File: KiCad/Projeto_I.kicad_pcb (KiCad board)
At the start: 2 copper layers, 16.5 x 21.5 mm, 3 parts

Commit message: AUla do dia 04/04/2025
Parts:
- added C1: 22p, Capacitor_THT:C_Rect_L7.0mm_W2.5mm_P5.00mm, F.Cu at (196.5, 100.5)
- added C10: 100n, Capacitor_THT:C_Rect_L7.0mm_W2.5mm_P5.00mm, F.Cu at (112.6, 87.9)
- added C11: 10u, Capacitor_THT:CP_Radial_D10.0mm_P3.80mm, F.Cu at (123.6, 78.9)
- added C2: 22p, Capacitor_THT:C_Rect_L7.0mm_W2.5mm_P5.00mm, F.Cu at (192.0, 81.0)
- added C3: 220n, Capacitor_THT:C_Rect_L7.0mm_W2.5mm_P5.00mm, F.Cu at (112.6, 63.6)
- added C4: 100n, Capacitor_THT:C_Rect_L7.0mm_W2.5mm_P5.00mm, F.Cu at (112.6, 67.7)
- added C5: 10n, Capacitor_THT:C_Rect_L7.0mm_W2.5mm_P5.00mm, F.Cu at (112.6, 71.7)
- added C6: 100n, Capacitor_THT:C_Rect_L7.0mm_W2.5mm_P5.00mm, F.Cu at (112.6, 75.8)
- added C7: 10n, Capacitor_THT:C_Rect_L7.0mm_W2.5mm_P5.00mm, F.Cu at (112.6, 79.8)
- added C8: 10u, Capacitor_THT:CP_Radial_D10.0mm_P3.80mm, F.Cu at (123.6, 67.4)
- added C9: 100n, Capacitor_THT:C_Rect_L7.0mm_W2.5mm_P5.00mm, F.Cu at (112.6, 83.9)
- added D1: RD0, LED_THT:LED_D3.0mm, F.Cu at (132.9, 64.3)
- added D2: RD0, LED_THT:LED_D3.0mm, F.Cu at (132.9, 69.8)
- added D3: RD0, LED_THT:LED_D3.0mm, F.Cu at (132.9, 75.3)
- added D4: RD0, LED_THT:LED_D3.0mm, F.Cu at (132.9, 80.8)
- added D5: RD0, LED_THT:LED_D3.0mm, F.Cu at (138.8, 64.3)
- added D6: RD0, LED_THT:LED_D3.0mm, F.Cu at (138.8, 69.8)
- added D7: D_Small, Diode_THT:D_DO-41_SOD81_P10.16mm_Horizontal, F.Cu at (129.8, 98.7)
- added D8: RD0, LED_THT:LED_D3.0mm, F.Cu at (138.8, 75.3)
- added F1: MF-MSMF050-2, Library:FUSM4632X85, F.Cu at (95.5, 116.6)
- added J1: PORTA, Connector_PinSocket_2.54mm:PinSocket_1x06_P2.54mm_Vertical, F.Cu at (102.4, 104.4)
- added J2: PORTB, Connector_PinSocket_2.54mm:PinSocket_1x08_P2.54mm_Vertical, F.Cu at (113.2, 104.9)
- added J3: PORTC, Connector_PinSocket_2.54mm:PinSocket_1x07_P2.54mm_Vertical, F.Cu at (117.8, 104.9)
- added J4: USB_B_Micro, Connector_USB:USB_Micro-AB_Molex_47590-0001, F.Cu at (233.2, 115.8)
- added J5: Barrel_Jack_Switch, Connector_BarrelJack:BarrelJack_Horizontal, F.Cu at (125.4, 95.3)
- added Q1: PMOS, Package_TO_SOT_THT:TO-92L_HandSolder, F.Cu at (93.4, 122.7)
- added R10: 10k, Resistor_THT:R_Axial_DIN0207_L6.3mm_D2.5mm_P7.62mm_Horizontal, F.Cu at (101.7, 100.1)
- added R4: 10K, Resistor_THT:R_Axial_DIN0207_L6.3mm_D2.5mm_P7.62mm_Horizontal, F.Cu at (101.7, 75.8)
- added R5: 10K, Resistor_THT:R_Axial_DIN0207_L6.3mm_D2.5mm_P7.62mm_Horizontal, F.Cu at (101.7, 79.8)
- added R6: 10K, Resistor_THT:R_Axial_DIN0207_L6.3mm_D2.5mm_P7.62mm_Horizontal, F.Cu at (101.7, 83.9)
- added R7: 10K, Resistor_THT:R_Axial_DIN0207_L6.3mm_D2.5mm_P7.62mm_Horizontal, F.Cu at (101.7, 87.9)
- added R8: 470, Resistor_THT:R_Axial_DIN0207_L6.3mm_D2.5mm_P7.62mm_Horizontal, F.Cu at (101.7, 92.0)
- added R9: 10k, Resistor_THT:R_Axial_DIN0207_L6.3mm_D2.5mm_P7.62mm_Horizontal, F.Cu at (101.7, 96.0)
- added SW1: reset, Button_Switch_THT:SW_TH_Tactile_Omron_B3F-10xx, F.Cu at (83.3, 115.6)
- added U1: PIC18F4550-IP, Package_DIP:DIP-40_W15.24mm, F.Cu at (204.8, 59.4)
- added U2: LM7805, Package_TO_SOT_THT:TO-220-3_Vertical, F.Cu at (134.5, 87.4)
- added U3: LM358, Package_DIP:DIP-8_W7.62mm, F.Cu at (132.7, 104.7)
- added U4: AMS1117, Package_TO_SOT_SMD:SOT-223-3_TabPin2, F.Cu at (125.0, 119.9)
- added Y1: 16MHz, Crystal:Crystal_HC49-U_Vertical, F.Cu at (198.5, 93.5)
- R1: value 10k -> 10K
- R2: value 1k -> 10K
- R3: value 100 -> 10K
- moved R3 16.3 mm to (101.7, 71.7)
- moved R2 14.5 mm to (101.7, 67.7)
- moved R1 13.1 mm to (101.7, 63.6)
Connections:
- R1 pad 2: Earth -> Rst
- R2 pad 1: +5V -> RD0
- R2 pad 2: Earth -> Net-(D1-A)
- R3 pad 1: +5V -> RD1
- R3 pad 2: Earth -> Net-(D2-A)
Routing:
- net Earth: track 23.7 -> 69.8 mm
- net osc1: track 0.00 -> 15.9 mm
- net osc2: track 0.00 -> 15.4 mm
- net +5V: track 20.9 -> 19.2 mm
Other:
- board size 16.5 x 21.5 mm -> 103.5 x 64 mm

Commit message: Atualização da PCB
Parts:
- removed U2: LM7805, Package_TO_SOT_THT:TO-220-3_Vertical
- added D9: RD0, LED_THT:LED_D3.0mm, F.Cu at (89.4, 47.0)
- added U5: USBLC6-2SC6, Package_TO_SOT_SMD:SOT-23-6, F.Cu at (77.9, 84.3)
- added U6: AMS1117-5.0, Package_TO_SOT_SMD:SOT-223-3_TabPin2, F.Cu at (74.8, 108.9)
- C1, C2: footprint Capacitor_THT:C_Rect_L7.0mm_W2.5mm_P5.00mm -> Capacitor_THT:C_Disc_D5.0mm_W2.5mm_P2.50mm
- C11, C8: footprint Capacitor_THT:CP_Radial_D10.0mm_P3.80mm -> Capacitor_THT:CP_Radial_D5.0mm_P2.50mm
- J4: value USB_B_Micro -> USB
- Q1: footprint Package_TO_SOT_THT:TO-92L_HandSolder -> Package_TO_SOT_SMD:SOT-23
- moved J4 168.8 mm to (67.7, 83.1), turned to -90 degrees
- moved R5 154.1 mm to (254.0, 103.4), turned to -90 degrees
- moved R4 147.9 mm to (247.0, 103.5), turned to -90 degrees
- moved R7 139.1 mm to (240.0, 103.0), turned to -90 degrees
- moved R6 132.7 mm to (233.0, 103.2), turned to -90 degrees
- moved R3 128.2 mm to (225.9, 103.4), turned to -90 degrees
- moved D4 124.0 mm to (251.5, 117.0)
- moved R2 122.8 mm to (219.0, 103.9), turned to -90 degrees
- moved C10 119.5 mm to (227.5, 55.0)
- moved D3 119.1 mm to (244.5, 117.1)
- moved D6 109.4 mm to (237.5, 117.0)
- moved D5 105.7 mm to (230.5, 117.0)
- moved D2 102.1 mm to (223.5, 117.0)
- moved D1 98.8 mm to (216.5, 117.0)
- moved J3 96.3 mm to (209.6, 76.0), turned to -90 degrees
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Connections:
- F1 pad 2: +5V -> USB_VCC
- J4 pad 2: RC4 -> /USB_D-
- J4 pad 3: RC5 -> /USB_D+
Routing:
- net Earth: track 69.8 -> 0.00 mm
- net +5V: track 19.2 -> 0.00 mm
- net osc1: track 15.9 -> 0.00 mm
- net osc2: track 15.4 -> 0.00 mm
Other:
- board size 103.5 x 64 mm -> 149 x 63.5 mm

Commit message: Atualização PCB
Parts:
- removed D9: RD0, LED_THT:LED_D3.0mm
- moved C10 92.4 mm to (138.0, 78.0), turned to -90 degrees
- moved C3 84.8 mm to (131.0, 73.0), turned to -90 degrees
- moved C8 80.5 mm to (151.0, 103.5), turned to -90 degrees
- moved C11 76.5 mm to (150.0, 95.0)
- moved SW1 75.9 mm to (150.0, 116.5)
- moved D8 58.3 mm to (137.0, 69.0)
- moved D7 52.0 mm to (136.5, 103.2)
- moved J4 50.2 mm to (116.2, 70.2)
- moved U6 50.1 mm to (124.5, 102.0)
- moved U4 49.9 mm to (124.2, 89.5)
- moved U5 49.6 mm to (125.9, 71.8)
- moved J5 49.1 mm to (127.5, 113.5)
- moved R1 47.2 mm to (134.9, 120.0), turned to 0 degrees
- moved Q1 46.5 mm to (131.5, 82.4)
- moved F1 42.8 mm to (124.0, 79.0), turned to -90 degrees
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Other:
- board size 149 x 63.5 mm -> 128 x 63.5 mm

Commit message: Finalizção da PCB v1.1
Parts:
- U4: value AMS1117 -> AMS1117-3.3
- moved C2 2.12 mm to (188.0, 119.5)
- moved C1 1.95 mm to (201.0, 117.0)
- moved Y1 1.50 mm to (197.0, 110.5)
- moved J4 0.30 mm to (116.5, 70.2)
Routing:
- net +5V: track 0.00 -> 177.4 mm, vias 0 -> 1
- net Vusb: track 0.00 -> 108.0 mm, vias 0 -> 1
- net RC4: track 0.00 -> 104.8 mm
- net RC0: track 0.00 -> 103.0 mm
- net RC5: track 0.00 -> 99.8 mm
- net RC1: track 0.00 -> 98.0 mm
- net RC2: track 0.00 -> 91.7 mm
- net Earth: track 0.00 -> 41.3 mm
- net +3.3V: track 0.00 -> 40.7 mm
- net Rst: track 0.00 -> 35.4 mm
- net PwrIn: track 0.00 -> 32.7 mm
- net RD5: track 0.00 -> 28.4 mm
- net RC7: track 0.00 -> 25.8 mm
- net RC6: track 0.00 -> 25.8 mm
- net Net-(D7-K): track 0.00 -> 24.9 mm
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- added copper zone on B.Cu, net Earth
- added copper zone on F.Cu, net Earth
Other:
- board size 128 x 63.5 mm -> 123 x 63.5 mm

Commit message: .
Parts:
- added J6: Alimentação, Connector_PinSocket_2.54mm:PinSocket_1x04_P2.54mm_Vertical, F.Cu at (189.8, 122.0)
- D2: value RD0 -> RD1
- D3: value RD0 -> RD4
- D4: value RD0 -> RD5
- D5: value RD0 -> RD2
- D6: value RD0 -> RD3
- Q1: value PMOS -> FDN340P
- U4: value AMS1117-3.3 -> AMS1117
- moved C1 4.80 mm to (197.2, 114.0)
- moved C2 3.47 mm to (189.8, 116.5)
- moved C8 2.94 mm to (150.1, 106.3), turned to 0 degrees
- moved Y1 2.39 mm to (195.7, 108.5)
- moved R1 1.01 mm to (134.7, 121.0)
- moved C6 0.56 mm to (180.0, 113.2)
- moved C7 0.54 mm to (180.0, 108.3)
- moved D2 0.12 mm to (231.9, 113.7)
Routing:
- net +5V: track 177.4 -> 255.2 mm, vias 1 -> 0
- net +3.3V: track 40.7 -> 93.5 mm
- net Earth: track 41.3 -> 18.8 mm
- net Vusb: track 108.0 -> 103.2 mm, vias 1 -> 0
- net osc2: track 16.3 -> 12.0 mm
- net osc1: track 16.5 -> 12.8 mm
- net RD1: track 11.3 -> 13.6 mm
- net RC2: track 91.7 -> 92.9 mm
- net PwrIn: track 32.7 -> 33.7 mm
- net RD0: track 19.5 -> 20.2 mm
- net /USB_D-: track 5.31 -> 6.01 mm
- net /USB_D+: track 4.79 -> 5.49 mm
- net Net-(J4-VBUS): track 7.71 -> 8.41 mm
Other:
- board text added: "3.3V"
- board text added: "5V"
- board text added: "GND"
- board text added: "RA0"
- board text added: "RA1"
- board text added: "RA2"
- board text added: "RA3"
- board text added: "RA4"
- board text added: "RA5"
- board text added: "RB0"
- board text added: "RB1"
- board text added: "RB2"
- board text added: "RB3"
- board text added: "RB4"
- board text added: "RB5"
- board text added: "RB6"
- board text added: "RB7"
- board text added: "min: 7V max: 12V"

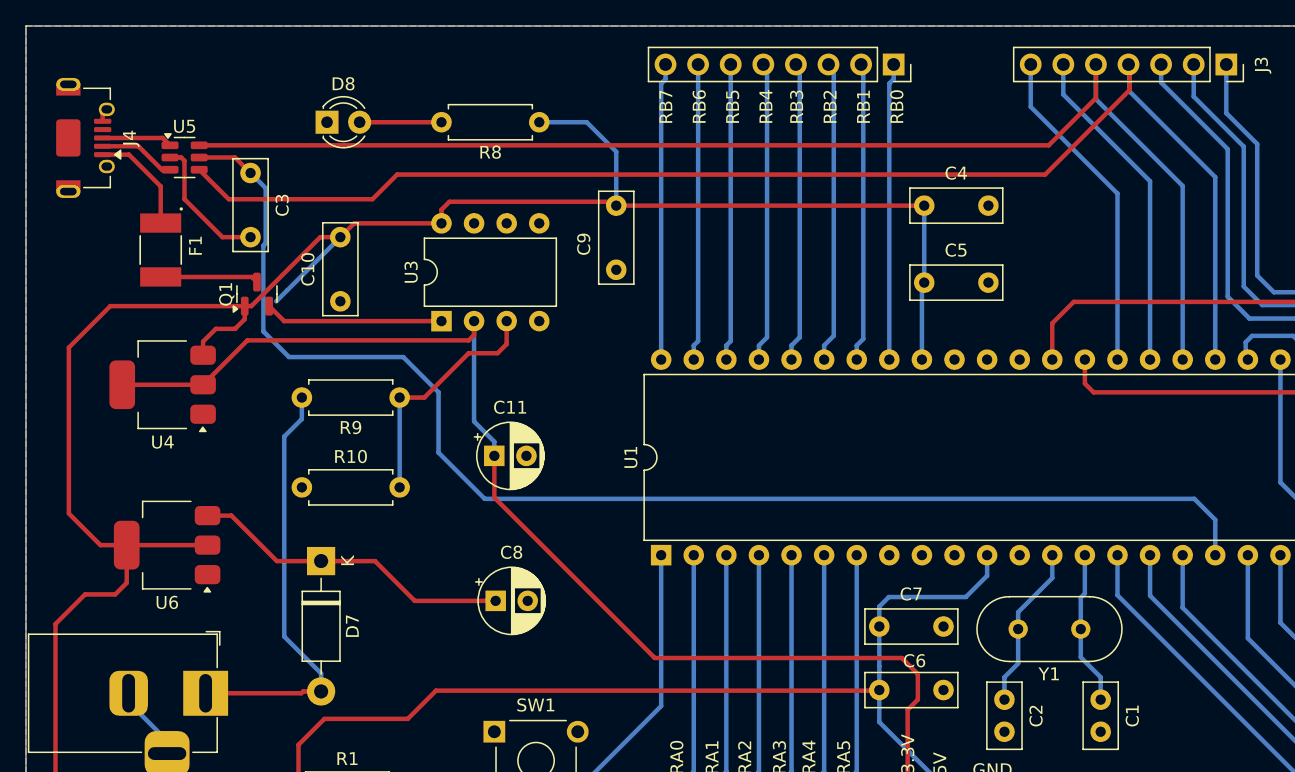
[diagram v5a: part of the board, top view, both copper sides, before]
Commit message: Atualização da PCB e conserto do esquemático do Transistor FDN340P
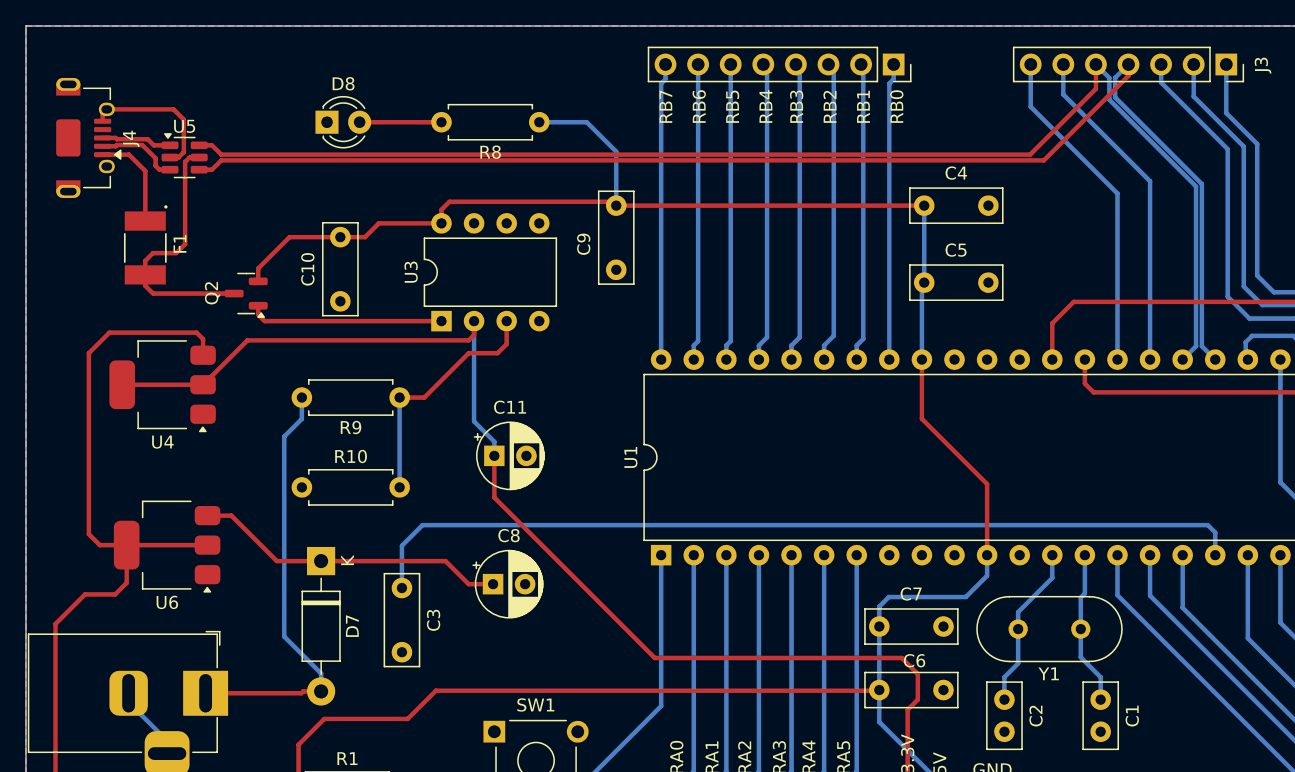
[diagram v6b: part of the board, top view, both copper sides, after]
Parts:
- removed Q1: FDN340P, Package_TO_SOT_SMD:SOT-23
- added Q2: FDN340P, Package_TO_SOT_SMD:SOT-23, F.Cu at (130.7, 82.3)
- moved C3 34.4 mm to (142.8, 105.3)
- moved C8 1.32 mm to (149.9, 105.0)
- moved F1 1.21 mm to (122.8, 78.8)
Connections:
- net RC4 renamed D-
- net RC5 renamed D+
- U5 pad 5: Vusb -> USB_VCC
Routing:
- net Vusb: track 103.2 -> 69.3 mm
- net USB_VCC: track 7.67 -> 20.4 mm
- net D-: track 104.8 -> 103.2 mm
- net +5V: track 255.2 -> 253.6 mm
- net Net-(Q2-G): track 13.9 -> 15.2 mm
- net D+: track 99.8 -> 100.9 mm
- net Net-(D7-K): track 25.2 -> 24.5 mm
- net Net-(J4-VBUS): track 8.41 -> 7.75 mm
- net Earth: track 18.8 -> 18.2 mm

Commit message: Commit
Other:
- board text added: "RC0"
- board text added: "RC1"
- board text added: "RC2"
- board text added: "RC4"
- board text added: "RC5"
- board text added: "RC6"
- board text added: "RC7"
- board text added: "Reset"
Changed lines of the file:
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@@
 			(solder_mask_margin 0.102)
 		)
+		(model "C:/Users/carlo/OneDrive/Área de Trabalho/projeti/Projeto_I/Arquivos/MSMF050/MF-MSMF050-2.step"
+			(offset
+				(xyz 0 0 1)
+			)
+			(scale
+				(xyz 1 1 1)
+			)
+			(rotate
+				(xyz 90 0 0)
+			)
+		)
 	)
 	(footprint "Connector_PinSocket_2.54mm:PinSocket_1x07_P2.54mm_Vertical"
@@
 			(at 3.25 -2.05 0)
 			(layer "F.SilkS")
+			(hide yes)
 			(effects
 				(font
@@
 			(pintype "passive")
 		)
-		(model "${KICAD8_3DMODEL_DIR}/Button_Switch_THT.3dshapes/SW_TH_Tactile_Omron_B3F-10xx.wrl"
+		(model "${KICAD8_3DMODEL_DIR}/Button_Switch_THT.3dshapes/SW_PUSH_6mm.step"
 			(offset
 				(xyz 0 0 0)
@@
 		(layer "Edge.Cuts")
 	)
+	(gr_text "RC7\n"
+		(at 191.85 68 90)
+		(layer "F.SilkS")
+		(effects
+			(font
+				(size 1 1)
+				(thickness 0.15)
+			)
+		)
+	)
 	(gr_text "RB3\n\n"
 		(at 174.4 67.8 90)
@@
 		)
 	)
+	(gr_text "RC1\n"
+		(at 204.5 68 90)
+		(layer "F.SilkS")
+		(effects
+			(font
+				(size 1 1)
+				(thickness 0.15)
+			)
+		)
+	)
 	(gr_text "RB4\n"
 		(at 171.2 67.8 90)
@@
 		)
 	)
+	(gr_text "RC0"
+		(at 207.1 68 90)
+		(layer "F.SilkS")
+		(effects
+			(font
+				(size 1 1)
+				(thickness 0.15)
+			)
+		)
+	)
 	(gr_text "RB2"
 		(at 176.2 67.8 90)
@@
 		)
 	)
+	(gr_text "RC5\n"
+		(at 197 68 90)
+		(layer "F.SilkS")
+		(effects
+			(font
+				(size 1 1)
+				(thickness 0.15)
+			)
+		)
+	)
 	(gr_text "GND\n"
 		(at 187.25 119.5 0)
@@
 		)
 	)
+	(gr_text "RC4\n"
+		(at 199.5 68 90)
+		(layer "F.SilkS")
+		(effects
+			(font
+				(size 1 1)
+				(thickness 0.15)
+			)
+		)
+	)
 	(gr_text "RB0"
 		(at 181.4 67.8 90)
@@
 		)
 	)
+	(gr_text "RC2\n\n"
+		(at 202.75 68 90)
+		(layer "F.SilkS")
+		(effects
+			(font
+				(size 1 1)
+				(thickness 0.15)
+			)
+		)
+	)
 	(gr_text "RA3"
 		(at 172.25 118.5 90)
@@
 		(layer "F.SilkS")
 		(effects
+			(font
+				(size 1 1)
+				(thickness 0.15)
+			)
+		)
+	)
+	(gr_text "Reset"
+		(at 153.25 114.5 0)
+		(layer "F.SilkS")
+		(effects
+			(font
+				(size 1 1)
+				(thickness 0.15)
+			)
+		)
+	)
+	(gr_text "RC6\n"
+		(at 194.25 68 90)
+		(layer "F.SilkS")
+		(effects

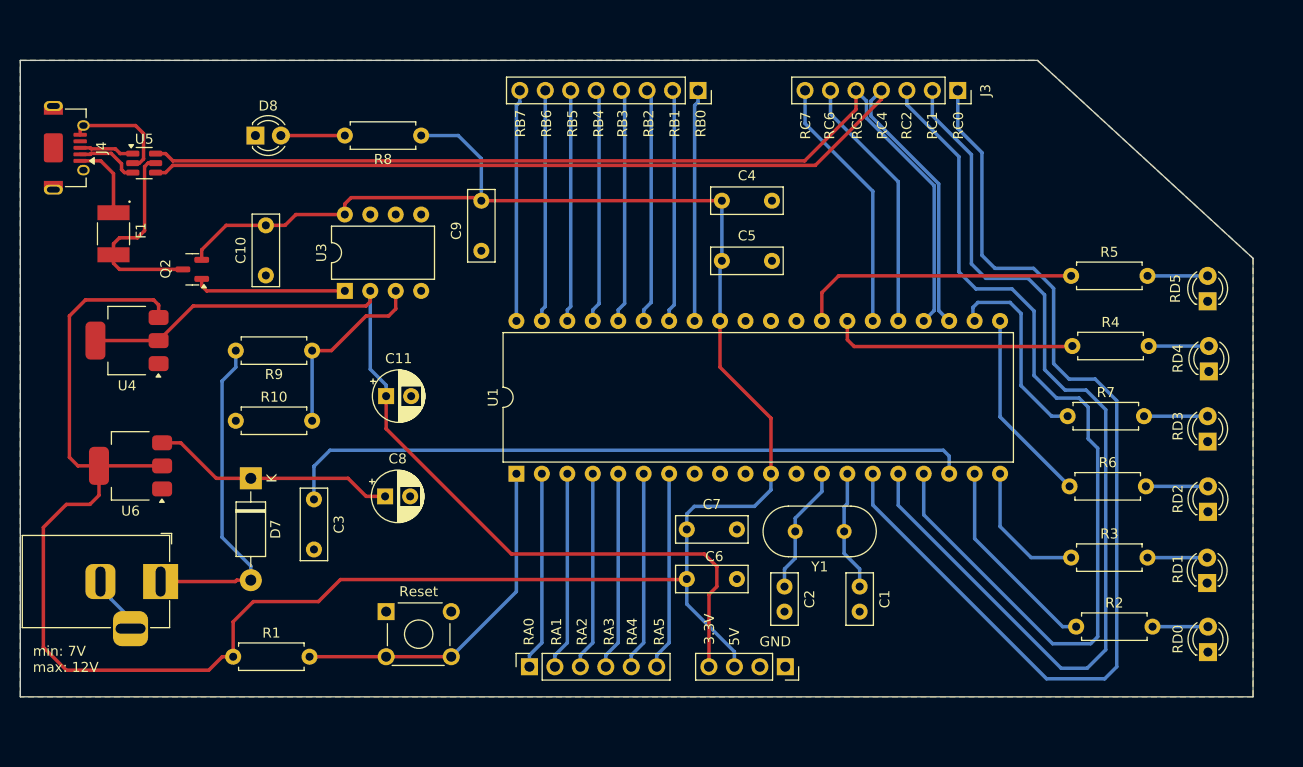
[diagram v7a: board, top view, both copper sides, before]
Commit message: Adicionado arquivos do Firmware com o programa de blink_led no RB4.
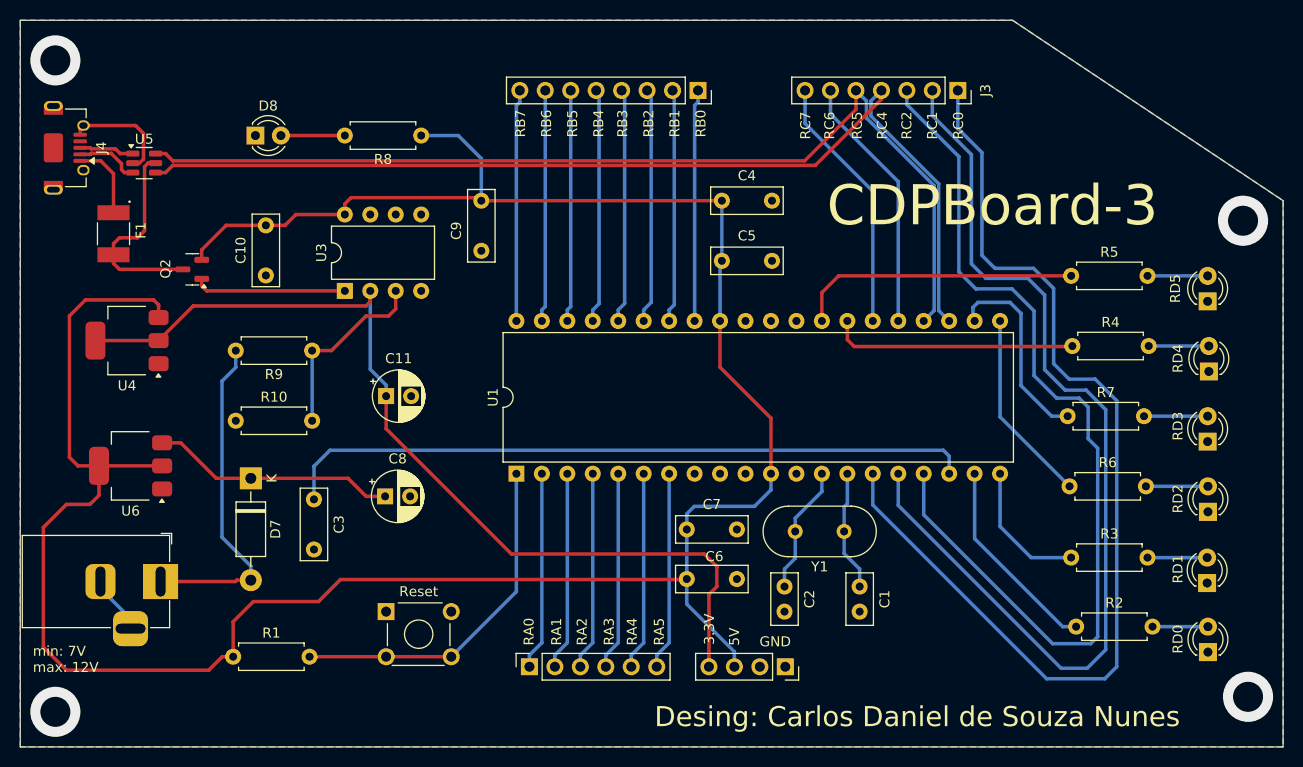
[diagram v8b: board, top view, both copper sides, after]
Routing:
- net (no net): vias 0 -> 4
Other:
- board size 123 x 63.5 mm -> 126 x 72.5 mm
- board text added: "CDPBoard-3"
- board text added: "Desing: Carlos Daniel de Souza Nunes"
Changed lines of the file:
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@@
 			(solder_mask_margin 0.102)
 		)
-		(model "C:/Users/carlo/OneDrive/Área de Trabalho/projeti/Projeto_I/Arquivos/MSMF050/MF-MSMF050-2.step"
+		(model "${KICAD8_3DMODEL_DIR}/Button_Switch_THT.3dshapes/MF-MSMF050-2.step"
 			(offset
 				(xyz 0 0 1)
@@
 	(gr_poly
 		(pts
-			(xy 215 61.5) (xy 236.5 81.25) (xy 236.5 125) (xy 113.5 125) (xy 113.5 61.5)
+			(xy 212.5 57.5) (xy 239.5 75.5) (xy 239.5 130) (xy 113.5 130) (xy 113.5 57.5)
 		)
 		(stroke
@@
 		)
 	)
+	(gr_text "Desing: Carlos Daniel de Souza Nunes"
+		(at 203 127 0)
+		(layer "F.SilkS")
+		(effects
+			(font
+				(size 2 2)
+				(thickness 0.3)
+			)
+		)
+	)
 	(gr_text "RB6\n"
 		(at 166 67.8 90)
@@
 		)
 	)
+	(gr_text "CDPBoard-3"
+		(at 210.5 76 0)
+		(layer "F.SilkS")
+		(effects
+			(font
+				(size 4 4)
+				(thickness 0.6)
+			)
+		)
+	)
+	(via
+		(at 235.5 77.5)
+		(size 5)
+		(drill 3)
+		(layers "F.Cu" "B.Cu")
+		(net 0)
+	)
+	(via
+		(at 117 126.5)
+		(size 5)
+		(drill 3)
+		(layers "F.Cu" "B.Cu")
+		(net 0)
+	)
+	(via
+		(at 236 125)
+		(size 5)
+		(drill 3)
+		(layers "F.Cu" "B.Cu")
+		(net 0)
+	)
+	(via
+		(at 117 61.5)
+		(size 5)
+		(drill 3)
+		(layers "F.Cu" "B.Cu")
+		(net 0)
+	)
 	(segment
 		(start 117.5 74.4)
@@
 		(polygon
 			(pts
-				(xy 113.5 61.5) (xy 215 61.5) (xy 236.5 81.25) (xy 236.5 125) (xy 113.5 125)
+				(xy 113.5 57.5) (xy 212.5 57.5) (xy 239.5 75.5) (xy 239.5 130) (xy 113.5 130)
 			)
 		)
